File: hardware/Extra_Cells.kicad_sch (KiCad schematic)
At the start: 2 parts

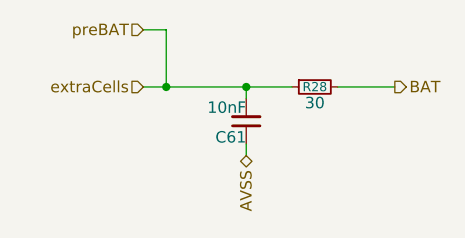
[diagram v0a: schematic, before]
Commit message: updated sheets, footprint, and calcs; 2nd review changes
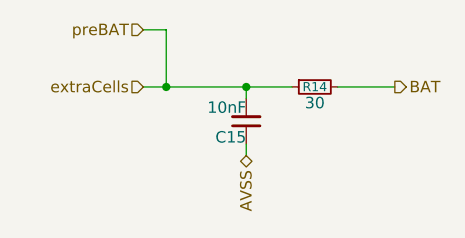
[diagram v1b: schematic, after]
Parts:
- renumbered C61 to C15, R28 to R14
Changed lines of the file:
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@@
 		(in_pos_files yes)
 		(dnp no)
-		(property "Reference" "C61"
+		(property "Reference" "C15"
 			(at 62.23 47.498 0)
 			(show_name no)
@@
 			(project "PS-SegmentMonitoringBoard"
 				(path "/f5c3f134-fd91-4d3b-aae6-719b554b2d69/4287d04b-d36d-432c-b4ed-46d8f5b465b5"
-					(reference "C61")
+					(reference "C15")
 					(unit 1)
 				)
@@
 		(in_pos_files yes)
 		(dnp no)
-		(property "Reference" "R28"
+		(property "Reference" "R14"
 			(at 69.85 41.91 90)
 			(show_name no)
@@
 			(project "PS-SegmentMonitoringBoard"
 				(path "/f5c3f134-fd91-4d3b-aae6-719b554b2d69/4287d04b-d36d-432c-b4ed-46d8f5b465b5"
-					(reference "R28")
+					(reference "R14")
 					(unit 1)
 				)
